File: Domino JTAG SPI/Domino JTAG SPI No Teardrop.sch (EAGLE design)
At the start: 17 parts, among them J1 MH10-1, J2 MH10-1, J3 MH2-1, J4 MH3-2, J5 MHRA7-2-0.1, SW1 IT-1124SMD

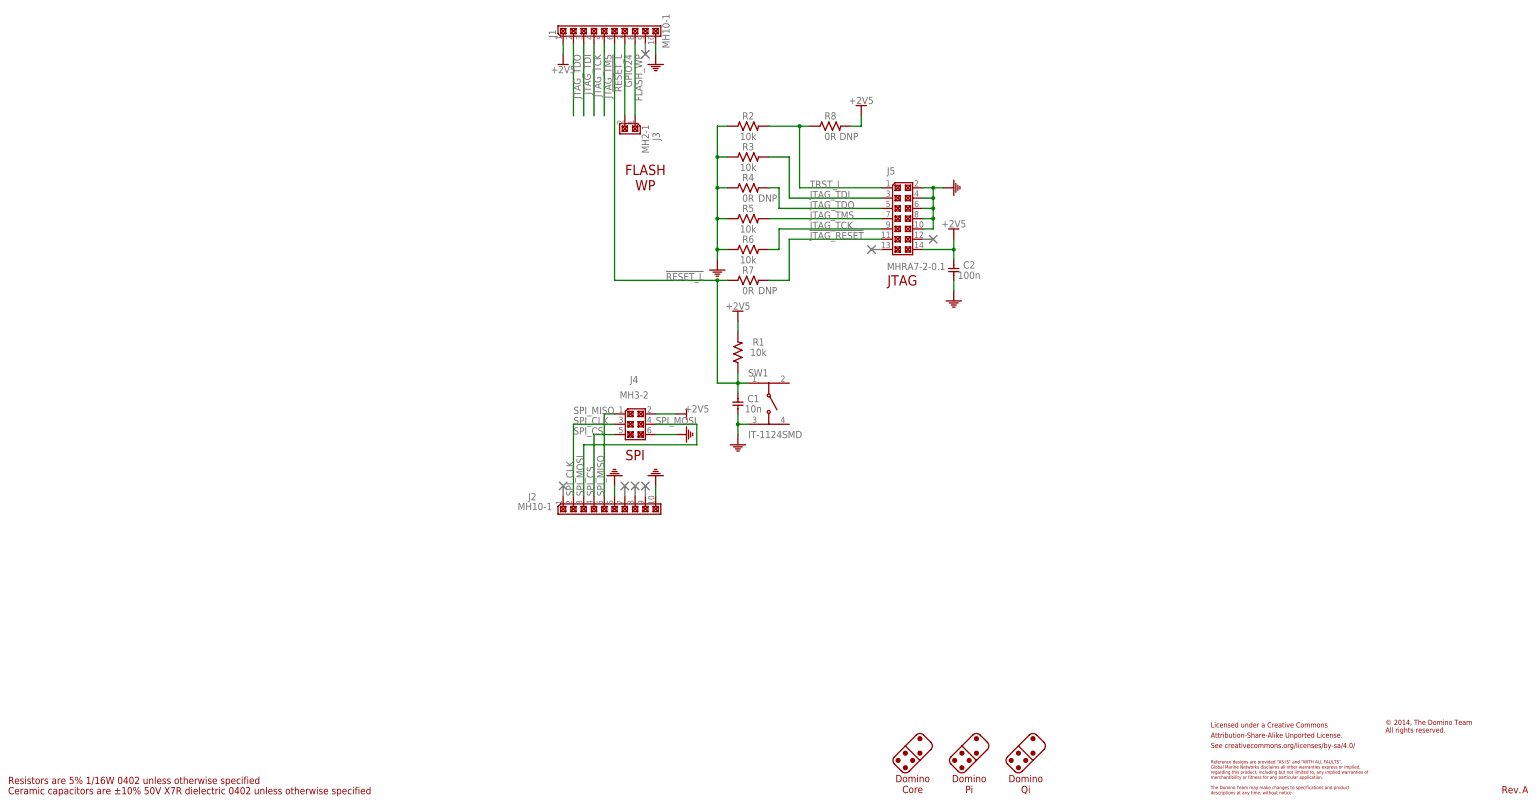
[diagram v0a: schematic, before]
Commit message: Modified Domino Flash SPI tile to fit a standard SPI Flash jig and SPI Flash chip footprint
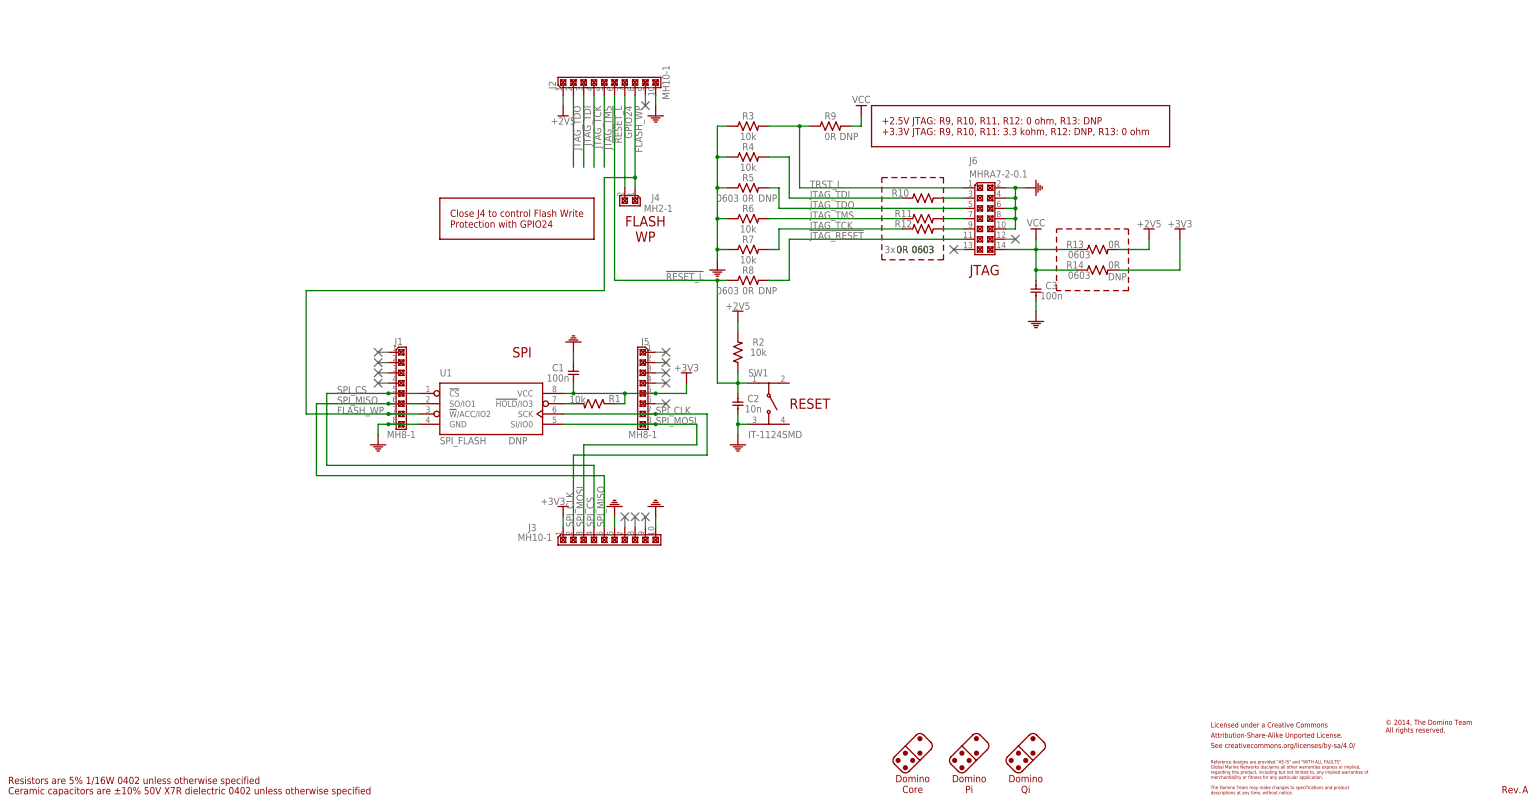
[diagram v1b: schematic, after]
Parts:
- added C3: 100n, Domino:CAP_0402
- added J6: MHRA7-2-0.1, Domino:MHRA7-2-0.1
- added R10, R11, R12, R13, R14, R9: 0R, Domino:RES_0603
- added U1: SPI_FLASH, Domino:SPI_FLASH
- C1: value 10n -> 100n; PARTNO C0402_10n_X7R_10%_CER_50V -> C0402_100n_X7R_10%_CER_50V
- C2: value 100n -> 10n; PARTNO C0402_100n_X7R_10%_CER_50V -> C0402_10n_X7R_10%_CER_50V
- J1: value MH10-1 -> MH8-1; device Domino:MH10-1 -> Domino:MH8-1; PARTNO MH10-1-0.1 -> MH8-1-0.1
- J3: value MH2-1 -> MH10-1; device Domino:MH2-1 -> Domino:MH10-1; PARTNO MH2-1-0.1 -> MH10-1-0.1
- J4: value MH3-2 -> MH2-1; device Domino:MH3-2 -> Domino:MH2-1; PARTNO MH3-2-0.1 -> MH2-1-0.1
- J5: value MHRA7-2-0.1 -> MH8-1; device Domino:MHRA7-2-0.1 -> Domino:MH8-1; PARTNO MHRA7-2-0.1 -> MH8-1-0.1
- R4, R7: value 0R -> 10k; device Domino:RES_0603 -> Domino:RES_0402; DNP T -> (none); PARTNO R0603_0R_5%_125mW -> R0402_10k_5%_62.5mW; RATE 125mW -> 62.5mW
- R5: value 10k -> 0R; device Domino:RES_0402 -> Domino:RES_0603; DNP (none) -> T; PARTNO R0402_10k_5%_62.5mW -> R0603_0R_5%_125mW; RATE 62.5mW -> 125mW
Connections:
- new net +3V3: C1.2, J3.1, J5.5, R1.1, R14.2, U1.VCC
- new net N$2: J6.7, R11.2
- new net N$3: J6.9, R12.2
- new net N$4: R1.2, U1.!HOLD!/IO3
- new net N$5: J6.3, R10.2
- new net VCC: C3.1, J6.14, R13.1, R14.1, R9.2
- net !JTAG_RESET: now also J6.11, R8.2; no longer J5.11, R7.2
- net !RESET_L: now also C2.1, J2.6, R2.1, R8.1; no longer C1.1, J1.6, R1.1, R7.1
- net +2V5: now also J2.1, R13.2, R2.2; no longer C2.1, J1.1, J4.2, J5.14, R1.2, R8.2
- net FLASH_WP: now also J1.7, J2.8, J4.1, U1.!W!/ACC/IO2; no longer J1.8, J3.1
- net GND: now also C1.1, C3.2, J1.8, J3.10, J3.6, J6.10, J6.2, J6.4, J6.6, J6.8, R7.1, U1.GND; no longer C1.2, J1.10, J2.6, J4.6, J5.10, J5.2, J5.4, J5.6, J5.8, R2.1
- net GPIO24: now also J2.7, J4.2; no longer J1.7, J3.2
- net JTAG_TCK: now also J2.4, R12.1, R7.2; no longer J1.4, J5.9, R6.2
- net JTAG_TDI: now also J2.3, R10.1, R4.2; no longer J1.3, J5.3, R3.2
- net JTAG_TDO: now also J2.2, J6.5, R5.2; no longer J1.2, J5.5, R4.2
- net JTAG_TMS: now also J2.5, R11.1, R6.2; no longer J1.5, J5.7, R5.2
- net SPI_CLK: now also J3.2, J5.7, U1.SCK; no longer J2.2, J4.3
- net SPI_CS: now also J1.5, J3.4, U1.!CS; no longer J2.4, J4.5
- net SPI_MISO: now also J1.6, J3.5, U1.SO/IO1; no longer J2.5, J4.1
- net SPI_MOSI: now also J3.3, J5.8, U1.SI/IO0; no longer J2.3, J4.4
- net TRST_L: now also J6.1, R3.2, R9.1; no longer J5.1, R2.2, R8.1
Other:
- note added: "+2.5V JTAG: R9, R10, R11, R12: 0 ohm, R13: DNP +3.3V JTAG: R9, R10, R11: 3.3 kohm, R12: DNP, R13: 0 ohm"
- note added: "3x"
- note added: "Close J4 to control Flash Write Protection with GPIO24"
- note added: "RESET"
- moved on the sheet: C1, C2, J2, R1, R2, R3, R4, R5, R6, R7, R8

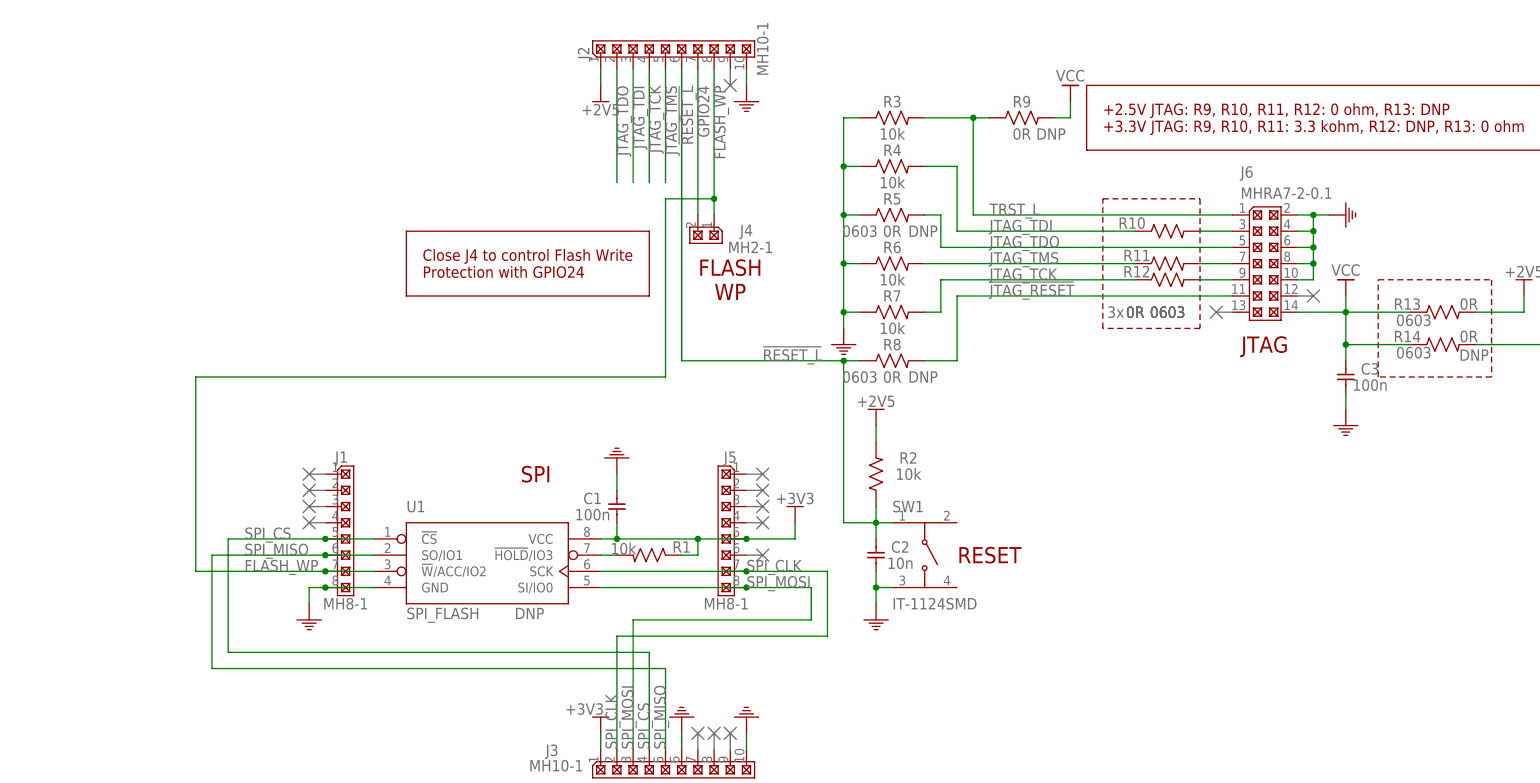
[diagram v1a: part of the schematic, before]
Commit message: Added series resistors on SPI Flash SO in Domino JTAG SPI tile
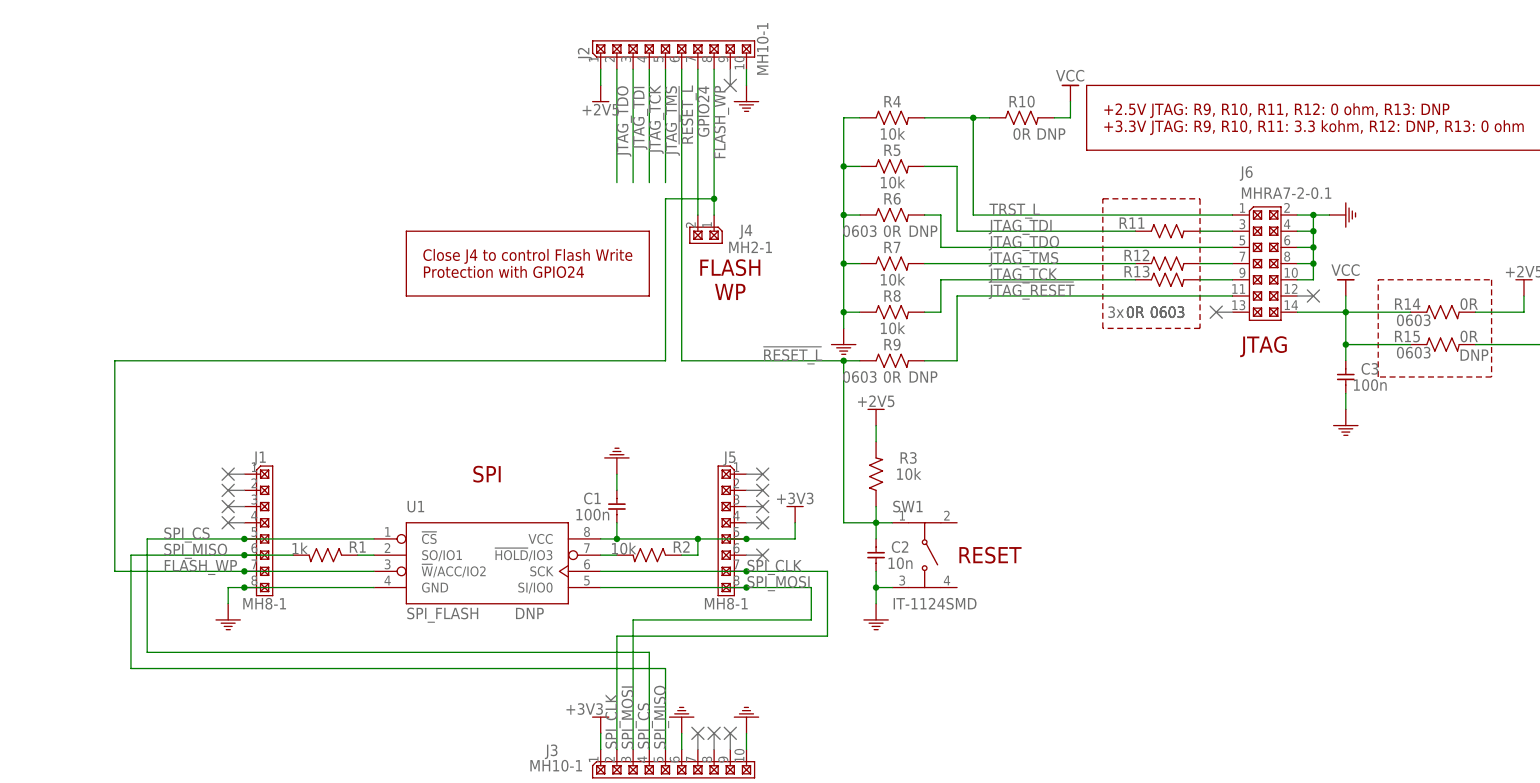
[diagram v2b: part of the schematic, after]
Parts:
- added R15: 0R, Domino:RES_0603
- R1: value 10k -> 1k; PARTNO R0402_10k_5%_62.5mW -> R0402_1k_5%_62.5mW
- R10: DNP (none) -> T
- R14: DNP T -> (none)
- R5, R8: value 0R -> 10k; device Domino:RES_0603 -> Domino:RES_0402; DNP T -> (none); PARTNO R0603_0R_5%_125mW -> R0402_10k_5%_62.5mW; RATE 125mW -> 62.5mW
- R6: value 10k -> 0R; device Domino:RES_0402 -> Domino:RES_0603; DNP (none) -> T; PARTNO R0402_10k_5%_62.5mW -> R0603_0R_5%_125mW; RATE 62.5mW -> 125mW
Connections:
- new net N$6: R1.1, U1.SO/IO1
- net !JTAG_RESET: now also R9.2; no longer R8.2
- net !RESET_L: now also R3.1, R9.1; no longer R2.1, R8.1
- net +2V5: now also R14.2, R3.2; no longer R13.2, R2.2
- net +3V3: now also R15.2, R2.1; no longer R1.1, R14.2
- net GND: now also R8.1; no longer R3.1
- net JTAG_TCK: now also R13.1, R8.2; no longer R12.1, R7.2
- net JTAG_TDI: now also R11.1, R5.2; no longer R10.1, R4.2
- net JTAG_TDO: now also R6.2; no longer R5.2
- net JTAG_TMS: now also R12.1, R7.2; no longer R11.1, R6.2
- net N$2: now also R12.2; no longer R11.2
- net N$3: now also R13.2; no longer R12.2
- net N$4: now also R2.2; no longer R1.2
- net N$5: now also R11.2; no longer R10.2
- net SPI_MISO: now also R1.2; no longer U1.SO/IO1
- net TRST_L: now also R10.1, R4.2; no longer R3.2, R9.1
- net VCC: now also R10.2, R15.1; no longer R13.1, R9.2
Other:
- moved on the sheet: J1, R1, R10, R11, R12, R13, R14, R2, R3, R4, R5, R6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

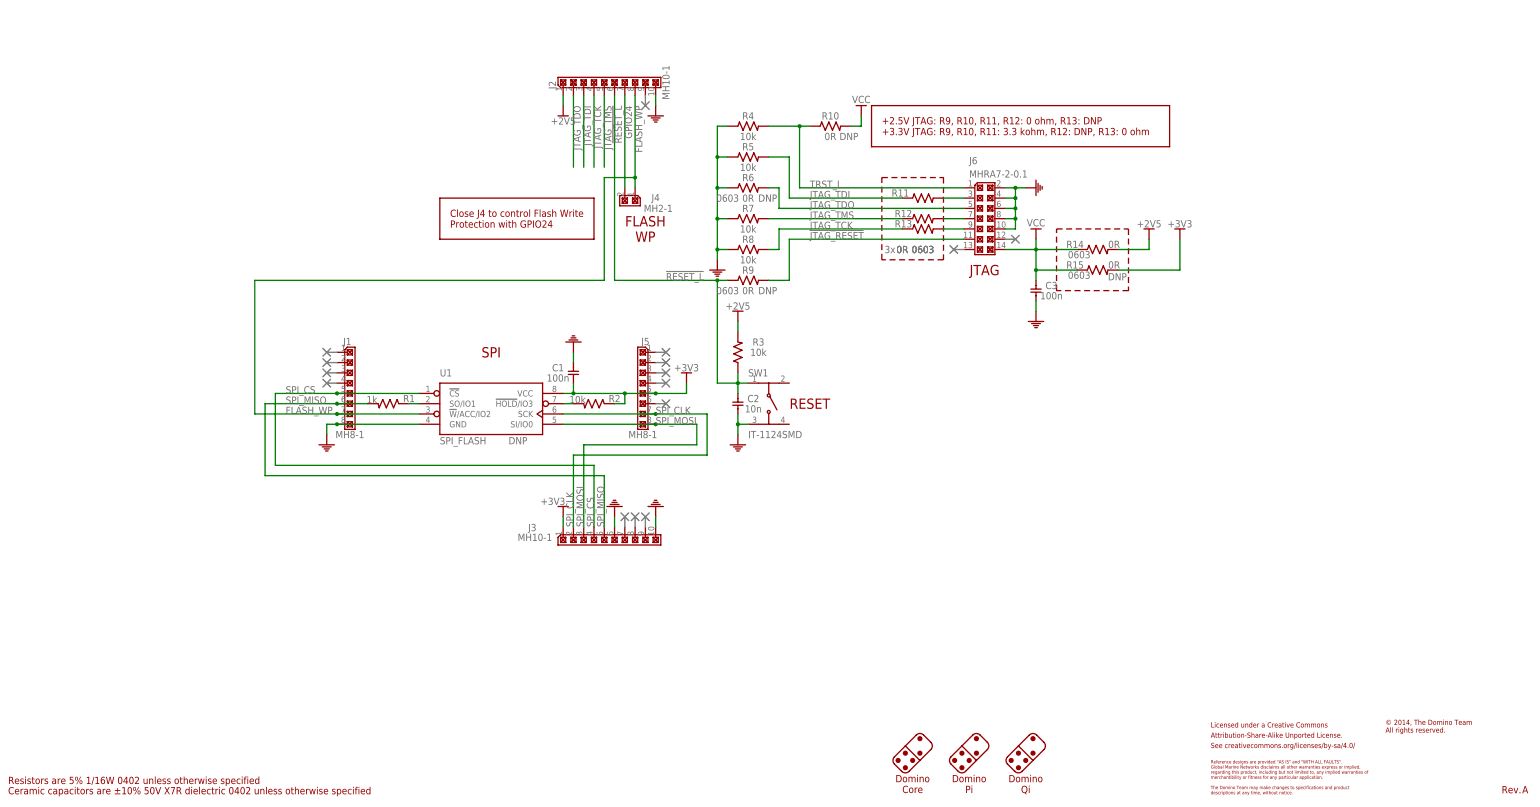
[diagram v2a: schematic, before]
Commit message: Changed Domino JTAG SPI to Rev. C
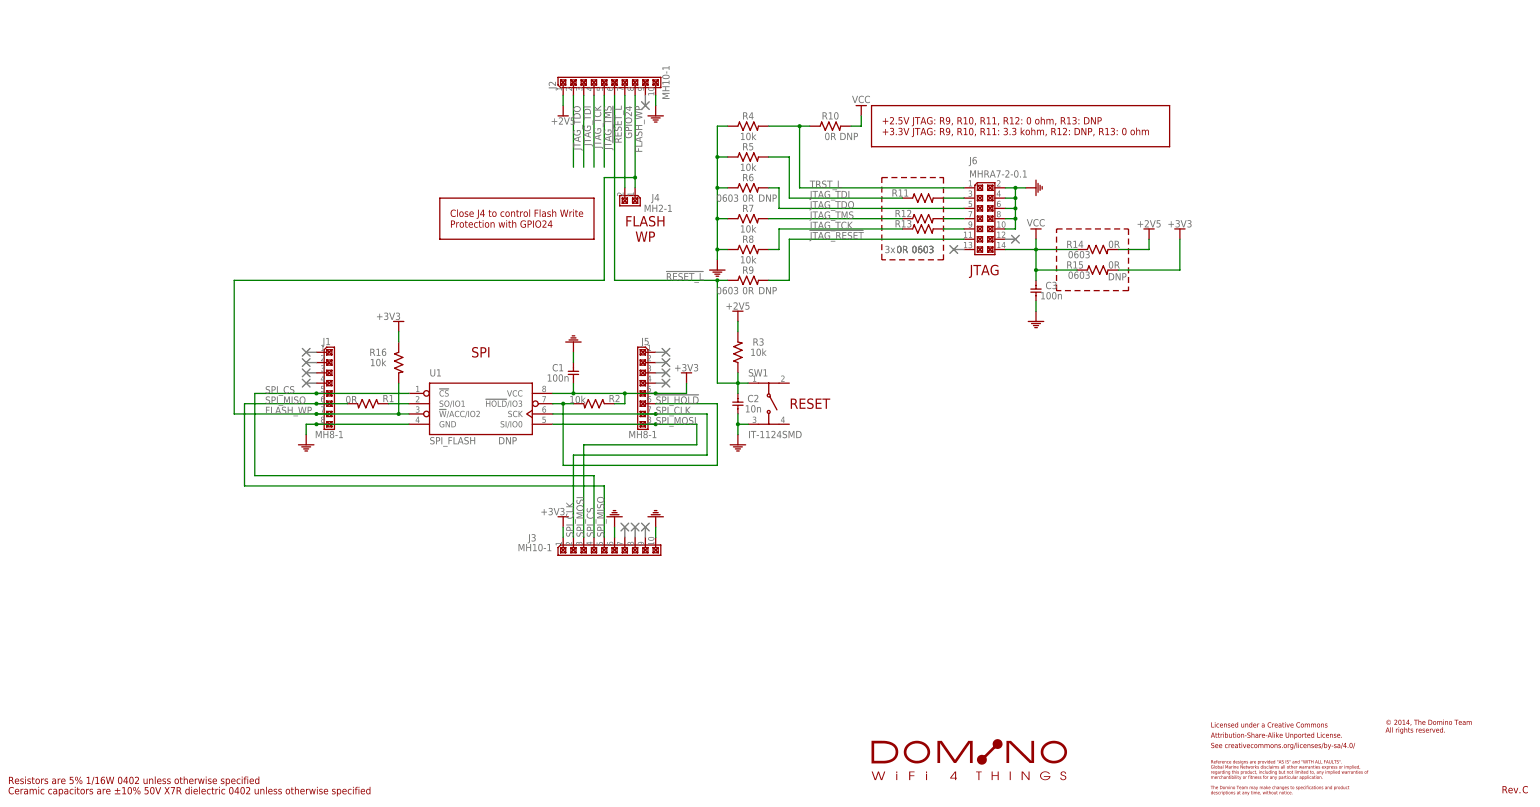
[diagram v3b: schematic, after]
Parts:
- added R16: 10k, Domino:RES_0402
- added U$2: DOMINO_LOGO_SMALL, Domino:DOMINO_LOGO_SMALL
- R1: value 1k -> 0R; PARTNO R0402_1k_5%_62.5mW -> R0402_0R_5%_62.5mW
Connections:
- removed net N$4: R2.2, U1.!HOLD!/IO3
- new net !SPI_HOLD: J5.6, R2.2, U1.!HOLD!/IO3
- net +3V3: now also R16.1
- net FLASH_WP: now also R16.2
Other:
- note removed: "Domino Core"
- note removed: "Domino Pi"
- note removed: "Domino Qi"
- moved on the sheet: J1, J3, R1, U1

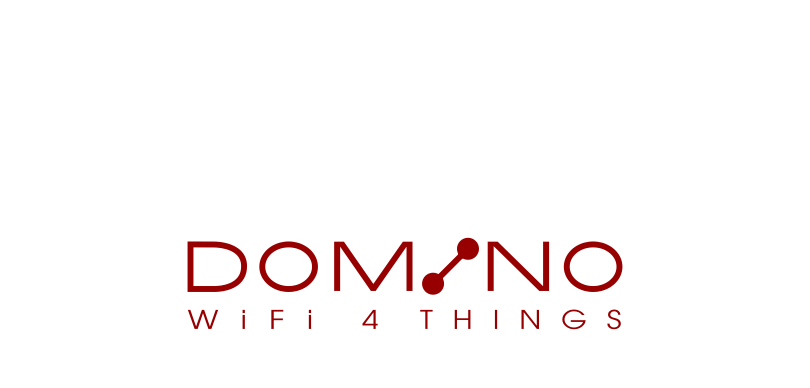
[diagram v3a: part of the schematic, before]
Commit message: Domino JTAG SPI Rev. C: changed Logos
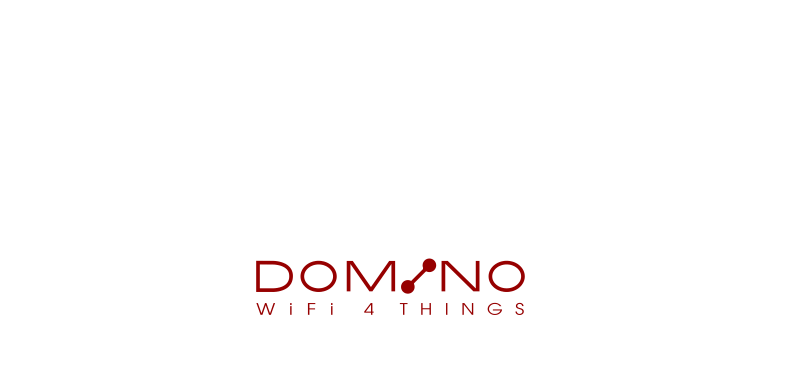
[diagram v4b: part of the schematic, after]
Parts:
- U$2: value DOMINO_LOGO_SMALL -> DOMINO_LOGO; device Domino:DOMINO_LOGO_SMALL -> Domino:DOMINO_LOGO; BOM EXCLUDE -> (none)
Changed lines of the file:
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@@
 <layer number="54" name="bGND_GNDA" color="1" fill="9" visible="no" active="no"/>
 <layer number="56" name="wert" color="7" fill="1" visible="no" active="no"/>
+<layer number="90" name="Modules" color="5" fill="1" visible="yes" active="yes"/>
 <layer number="91" name="Nets" color="2" fill="1" visible="yes" active="yes"/>
 <layer number="92" name="Busses" color="1" fill="1" visible="yes" active="yes"/>
@@
 </part>
 <part name="U$1" library="Domino" deviceset="+3V3" device=""/>
-<part name="U$2" library="Domino" deviceset="DOMINO_LOGO_SMALL" device="">
-<attribute name="BOM" value="EXCLUDE"/>
-</part>
+<part name="U$2" library="Domino" deviceset="DOMINO_LOGO" device=""/>
 </parts>
 <sheets>
@@
 <attribute name="VALUE" x="99.06" y="123.19" size="1.778" layer="96" align="center"/>
 </instance>
-<instance part="U$2" gate="G$1" x="218.44" y="12.7">
-<attribute name="BOM" x="218.44" y="12.7" size="1.778" layer="96" display="off"/>
-</instance>
+<instance part="U$2" gate="G$1" x="226.06" y="12.7"/>
 </instances>
 <busses>
